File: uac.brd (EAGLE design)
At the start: 100 x 100 mm, 201 parts, among them Q1 2N7002CK4SST, Q6 2N7002CK4SST, Q7 2N7002CK4SST, U2 ADXL345, Y1 RESONATORSMD

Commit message: Touch pad
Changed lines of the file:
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@@
 <wire x1="73.5" y1="12" x2="73" y2="12.5" width="0.2032" layer="16"/>
 <wire x1="73" y1="12.5" x2="71" y2="12.5" width="0.2032" layer="16"/>
-<polygon width="0.2032" layer="1" isolate="0.3048">
+<polygon width="0.2032" layer="1" isolate="0.3048" rank="2">
 <vertex x="0" y="0"/>
-<vertex x="0" y="11"/>
-<vertex x="100" y="11"/>
+<vertex x="0" y="100"/>
+<vertex x="100" y="100"/>
 <vertex x="100" y="0"/>
 </polygon>
@@
 <contactref element="U$1" pad="11"/>
 <polygon width="0.2032" layer="1">
-<vertex x="74" y="94"/>
-<vertex x="83" y="94" curve="-90"/>
-<vertex x="84" y="93"/>
-<vertex x="84" y="84" curve="-90"/>
-<vertex x="83" y="83"/>
-<vertex x="74" y="83" curve="-90"/>
-<vertex x="73" y="84"/>
-<vertex x="73" y="93" curve="-90"/>
+<vertex x="3" y="60"/>
+<vertex x="12" y="60" curve="-90"/>
+<vertex x="13" y="59"/>
+<vertex x="13" y="50" curve="-90"/>
+<vertex x="12" y="49"/>
+<vertex x="3" y="49" curve="-90"/>
+<vertex x="2" y="50"/>
+<vertex x="2" y="59" curve="-90"/>
 </polygon>
-<via x="78.5" y="88.5" extent="1-16" drill="0.31"/>
-<wire x1="78.5" y1="88.5" x2="45.05025" y2="53.181978125" width="0" layer="19" extent="1-1"/>
+<via x="7.5" y="54.5" extent="1-16" drill="0.31"/>
+<wire x1="7.5" y1="54.5" x2="45.05025" y2="53.181978125" width="0" layer="19" extent="1-1"/>
 </signal>
 <signal name="TOUCH3">
@@
 <contactref element="U$1" pad="57"/>
 <polygon width="0.2032" layer="1">
-<vertex x="35" y="99"/>
-<vertex x="44" y="99" curve="-90"/>
-<vertex x="45" y="98"/>
-<vertex x="45" y="89" curve="-90"/>
-<vertex x="44" y="88"/>
-<vertex x="35" y="88" curve="-90"/>
-<vertex x="34" y="89"/>
-<vertex x="34" y="98" curve="-90"/>
+<vertex x="46" y="99"/>
+<vertex x="55" y="99" curve="-90"/>
+<vertex x="56" y="98"/>
+<vertex x="56" y="89" curve="-90"/>
+<vertex x="55" y="88"/>
+<vertex x="46" y="88" curve="-90"/>
+<vertex x="45" y="89"/>
+<vertex x="45" y="98" curve="-90"/>
 </polygon>
-<via x="39.5" y="93.5" extent="1-16" drill="0.31"/>
-<wire x1="39.5" y1="93.5" x2="53.889084375" y2="54.242640625" width="0" layer="19" extent="1-1"/>
+<via x="50.5" y="93.5" extent="1-16" drill="0.31"/>
+<wire x1="50.5" y1="93.5" x2="53.889084375" y2="54.242640625" width="0" layer="19" extent="1-1"/>
 </signal>
 </signals>

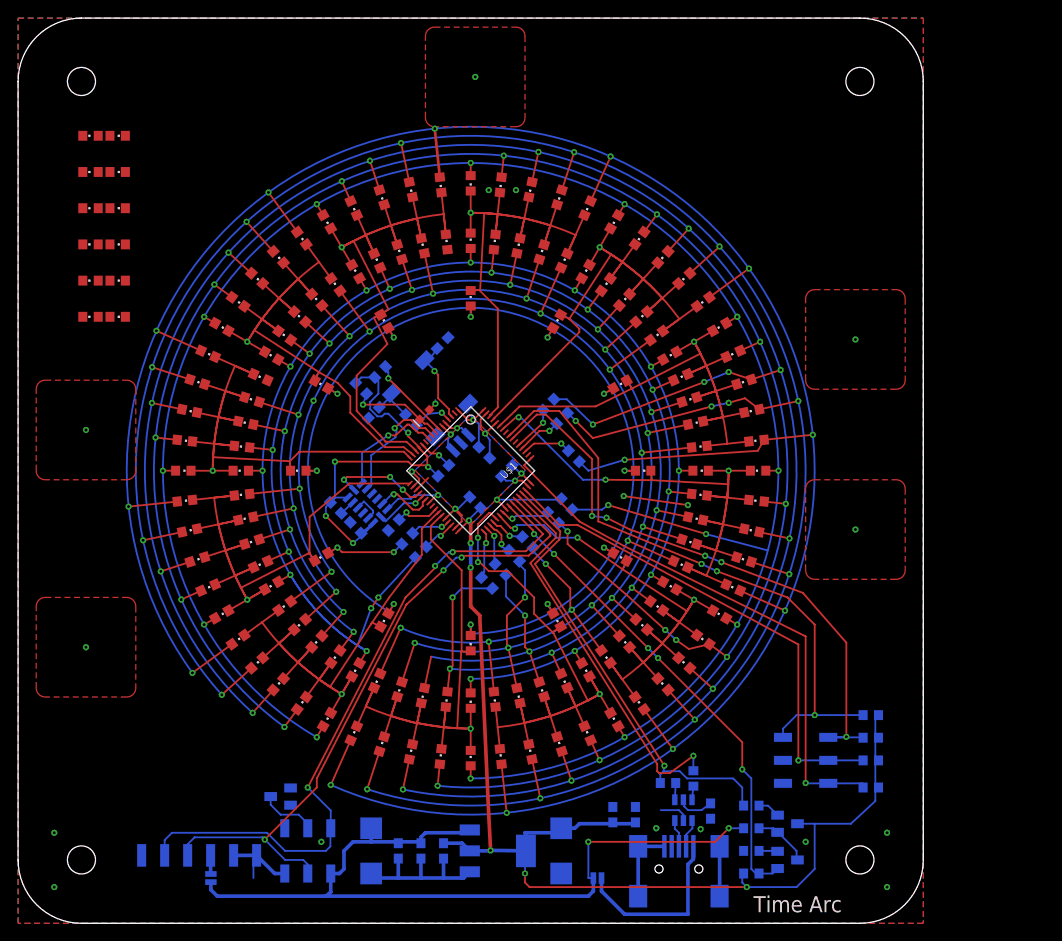
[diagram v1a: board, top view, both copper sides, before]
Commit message: touch pad place
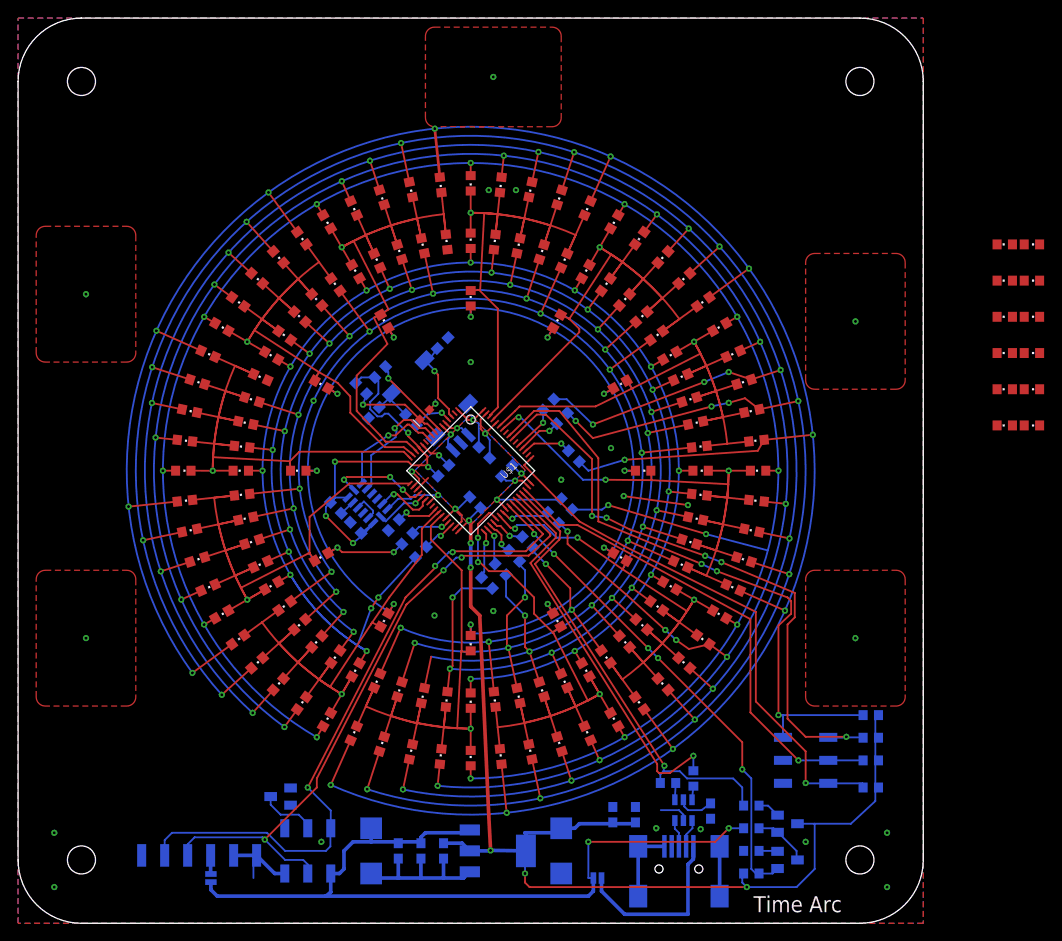
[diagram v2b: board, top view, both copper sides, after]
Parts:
- moved SPECIAL0 101.7 mm to (109.0, 75.0)
- moved SPECIAL1 101.7 mm to (109.0, 71.0)
- moved SPECIAL10 101.7 mm to (112.0, 71.0)
- moved SPECIAL11 101.7 mm to (112.0, 75.0)
- moved SPECIAL2 101.7 mm to (109.0, 67.0)
- moved SPECIAL3 101.7 mm to (109.0, 63.0)
- moved SPECIAL4 101.7 mm to (109.0, 59.0)
- moved SPECIAL5 101.7 mm to (109.0, 55.0)
- moved SPECIAL6 101.7 mm to (112.0, 55.0)
- moved SPECIAL7 101.7 mm to (112.0, 59.0)
- moved SPECIAL8 101.7 mm to (112.0, 63.0)
- moved SPECIAL9 101.7 mm to (112.0, 67.0)
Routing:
- net TDO: track 66.6 -> 69.6 mm
- net TCK: track 60.9 -> 59.7 mm
- net TMS: track 55.1 -> 54.1 mm
- net TRST: track 67.6 -> 68.5 mm
- net GND: vias 18 -> 23

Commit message: touch connected
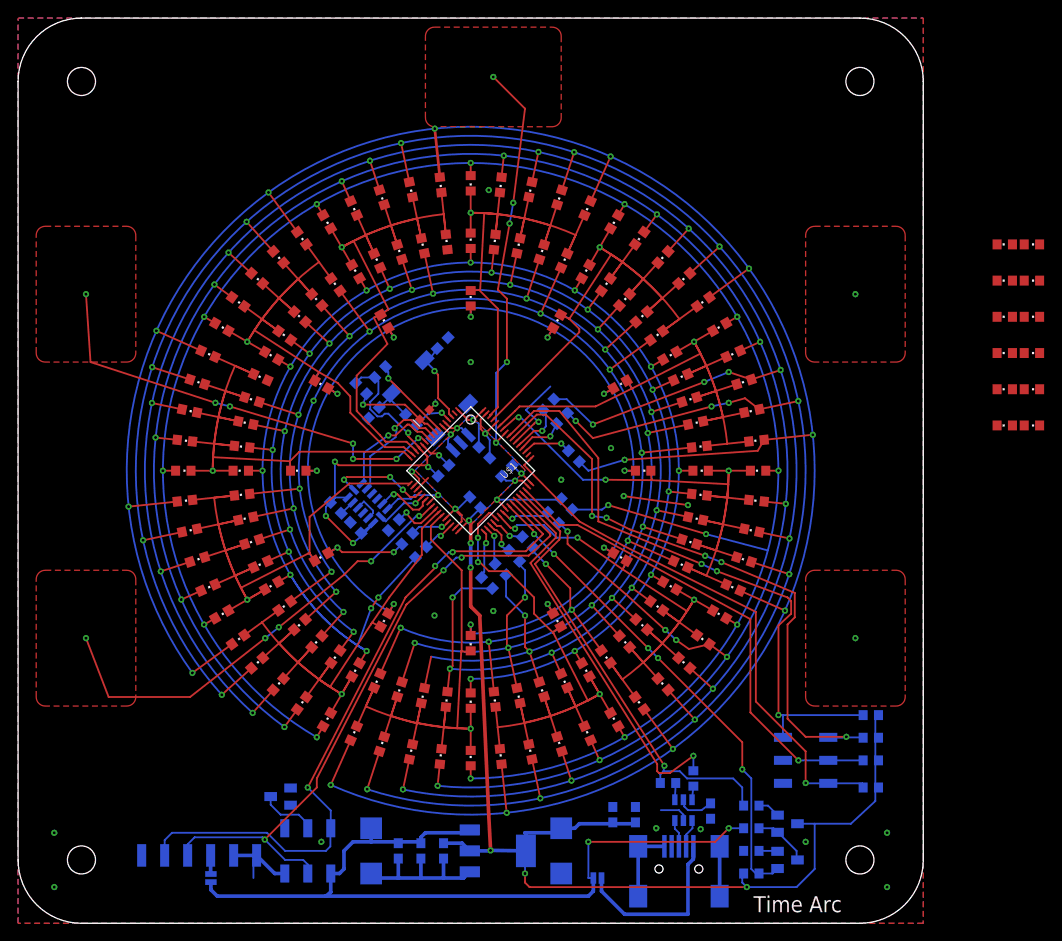
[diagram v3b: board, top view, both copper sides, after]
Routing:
- net TOUCH3: track 0.00 -> 50.7 mm, vias 1 -> 5
- net TOUCH2: track 0.00 -> 48.8 mm, vias 1 -> 7
- net TOUCH5: track 0.00 -> 44.6 mm, vias 1 -> 5
- net TOUCH4: track 0.00 -> 9.12 mm, vias 1 -> 2
- net N$15: track 5.06 -> 5.90 mm
- net N$35: track 4.91 -> 5.61 mm
- net GND: vias 23 -> 22

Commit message: last touch
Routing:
- net TOUCH1: track 0.00 -> 47.7 mm, vias 1 -> 5
- net TOUCH4: track 9.12 -> 45.7 mm, vias 2 -> 3
- net GND: track 83.7 -> 76.5 mm
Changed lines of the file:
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@@
 <wire x1="56.90104375" y1="41.09895625" x2="58.3" y2="39.7" width="0.2032" layer="16"/>
 <via x="58.3" y="39.7" extent="1-16" drill="0.31"/>
-<wire x1="58.3" y1="39.7" x2="61" y2="37" width="0.2032" layer="1"/>
-<wire x1="61" y1="37" x2="61" y2="34.7966" width="0.2032" layer="1"/>
+<wire x1="58.3" y1="39.7" x2="58" y2="39.3" width="0.2032" layer="1"/>
+<wire x1="58" y1="39.3" x2="61" y2="34.7966" width="0.2032" layer="1"/>
 <wire x1="61" y1="34.7966" x2="61.16791875" y2="34.62868125" width="0.2032" layer="1"/>
 <wire x1="57.728" y1="67.357359375" x2="65.37131875" y2="61.16791875" width="0" layer="19" extent="1-1"/>
 <wire x1="68.89591875" y1="51.986040625" x2="65.37131875" y2="61.16791875" width="0" layer="19" extent="1-1"/>
 <wire x1="67.357359375" y1="42.272" x2="68.89591875" y2="51.986040625" width="0" layer="19" extent="1-1"/>
-<wire x1="61" y1="37" x2="67.357359375" y2="42.272" width="0" layer="19" extent="1-1"/>
+<wire x1="58.3" y1="39.7" x2="67.357359375" y2="42.272" width="0" layer="19" extent="16-16"/>
 <wire x1="51.986040625" y1="31.10408125" x2="61" y2="34.7966" width="0" layer="19" extent="1-1"/>
 <wire x1="42.272" y1="32.642640625" x2="51.986040625" y2="31.10408125" width="0" layer="19" extent="1-1"/>
@@
 <wire x1="49" y1="45.1" x2="48.3" y2="45.8" width="0.2032" layer="1"/>
 <wire x1="36.97365625" y1="46.470709375" x2="35.70104375" y2="45.29895625" width="0.2032" layer="16"/>
-<via x="74" y="46.2" extent="1-16" drill="0.31"/>
-<wire x1="74" y1="46.2" x2="66.9" y2="47.2" width="0.2032" layer="1"/>
-<via x="66.9" y="47.2" extent="1-16" drill="0.31"/>
 <wire x1="45.430328125" y1="56.730328125" x2="46.1" y2="57.4" width="0.2032" layer="1"/>
 <via x="46.1" y="57.4" extent="1-16" drill="0.31"/>
@@
 <via x="52.5" y="34.5" extent="1-16" drill="0.31"/>
 <via x="65.5" y="52.5" extent="1-16" drill="0.31"/>
+<via x="62" y="39.3" extent="1-16" drill="0.31"/>
+<via x="60.5" y="37.5" extent="1-16" drill="0.31"/>
 <wire x1="39.2" y1="45.6" x2="43.6360375" y2="48.23223125" width="0" layer="19" extent="1-16"/>
+<wire x1="60.5" y1="37.5" x2="52.5" y2="34.5" width="0" layer="19" extent="1-1"/>
 </signal>
 <signal name="+3V3">
@@
 </polygon>
 <via x="92.5" y="31.5" extent="1-16" drill="0.31"/>
-<wire x1="92.5" y1="31.5" x2="56.363959375" y2="51.767765625" width="0" layer="19" extent="1-1"/>
+<wire x1="56.363959375" y1="51.767765625" x2="57" y2="52.4" width="0.2032" layer="1"/>
+<wire x1="57" y1="52.4" x2="57.4" y2="52.4" width="0.2032" layer="1"/>
+<wire x1="57.4" y1="52.4" x2="62.6" y2="47.8" width="0.2032" layer="1"/>
+<via x="62.6" y="47.8" extent="1-16" drill="0.31"/>
+<wire x1="62.6" y1="47.8" x2="65" y2="47.8" width="0.2032" layer="16"/>
+<via x="65" y="47.8" extent="1-16" drill="0.31"/>
+<wire x1="65" y1="47.8" x2="77.3" y2="45.6" width="0.2032" layer="1"/>
+<via x="77.3" y="45.6" extent="1-16" drill="0.31"/>
+<wire x1="77.3" y1="45.6" x2="79.1" y2="45.3" width="0.2032" layer="16"/>
+<via x="79.1" y="45.3" extent="1-16" drill="0.31"/>
+<wire x1="79.1" y1="45.3" x2="87" y2="44" width="0.2032" layer="1"/>
+<wire x1="87" y1="44" x2="87" y2="37" width="0.2032" layer="1"/>
+<wire x1="87" y1="37" x2="92.5" y2="31.5" width="0.2032" layer="1"/>
 </signal>
 <signal name="TOUCH2">
@@
 <wire x1="57.5" y1="55.4" x2="56.1" y2="56.7" width="0.2032" layer="16"/>
 <wire x1="56.1" y1="56.7" x2="58.8" y2="59.3" width="0.2032" layer="16"/>
-<wire x1="92.5" y1="69.5" x2="58.8" y2="59.3" width="0" layer="19" extent="16-16"/>
+<wire x1="58.8" y1="59.3" x2="59.5" y2="60" width="0.2032" layer="16"/>
+<wire x1="59.5" y1="60" x2="60" y2="60" width="0.2032" layer="16"/>
+<via x="60" y="60" extent="1-16" drill="0.31"/>
+<wire x1="60" y1="60" x2="65" y2="60" width="0.2032" layer="1"/>
+<wire x1="65" y1="60" x2="80.9" y2="69.4" width="0.2032" layer="1"/>
+<wire x1="80.9" y1="69.4" x2="92.5" y2="69.5" width="0.2032" layer="1"/>
 </signal>
 <signal name="TOUCH5">
